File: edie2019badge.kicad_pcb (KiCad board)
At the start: 2 copper layers, 90 x 95.7 mm, 52 parts, among them CN2 2x2, CN3 2x2, CN4 2x2, CN5 1x6_vertical_sm, IC1 ESP-32-WROOM, IC2 AMS1117-3.3, SW1 switch_3x6, SW2 switch_3x6, SW3 switch_3x6

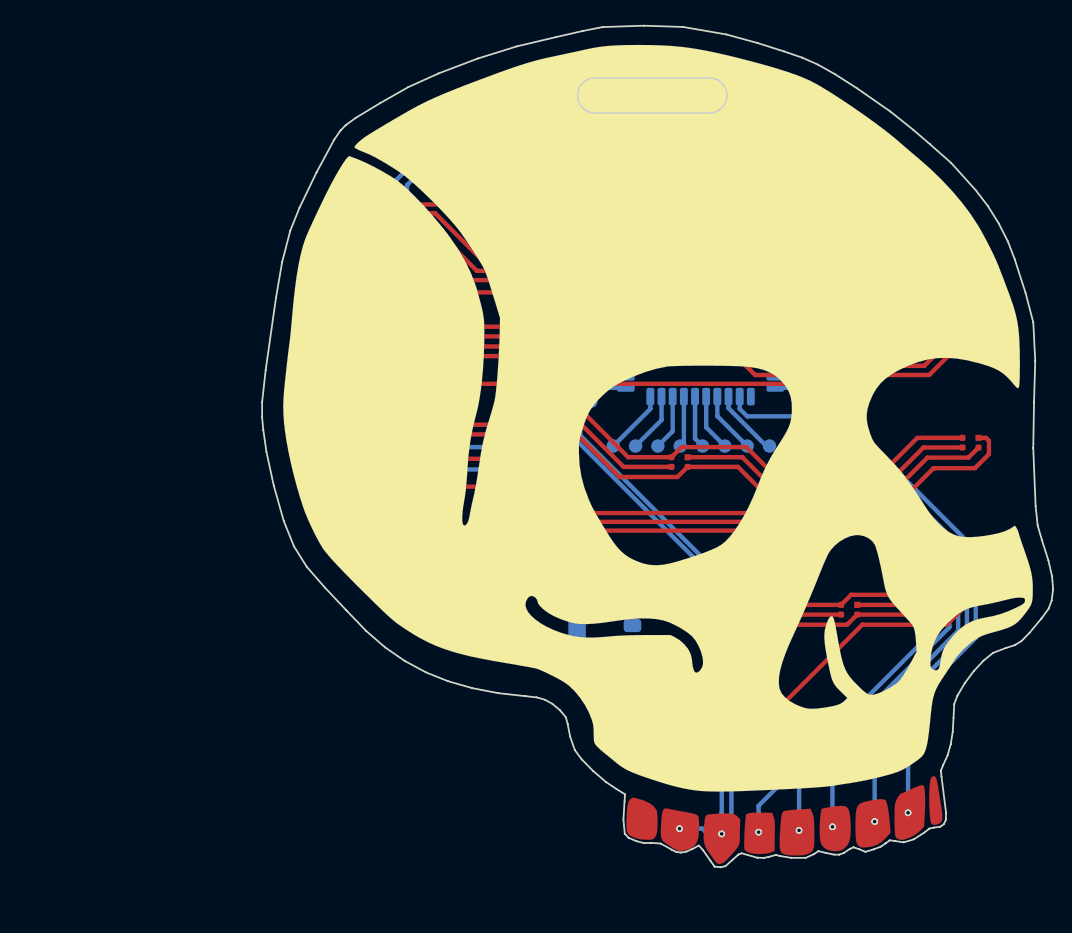
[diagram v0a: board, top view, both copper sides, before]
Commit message: trace layout complete for now, still missing some footprints
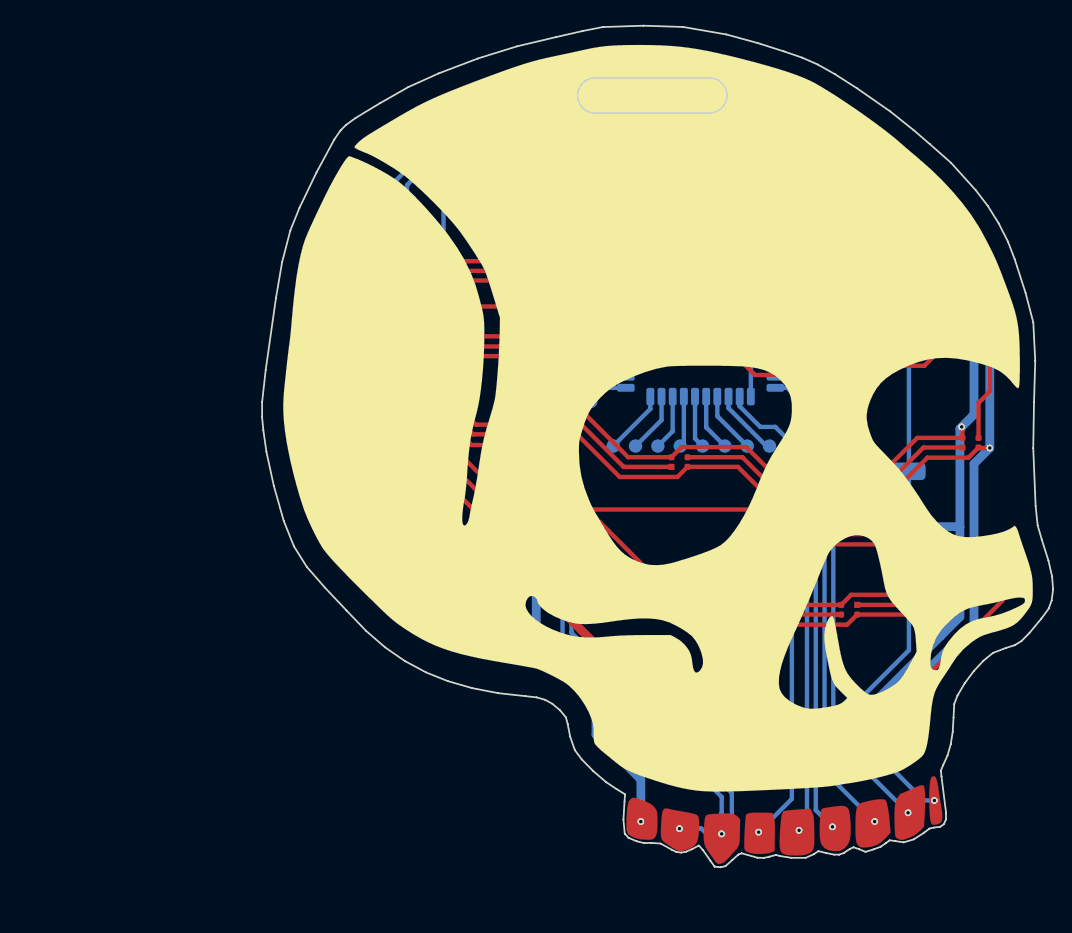
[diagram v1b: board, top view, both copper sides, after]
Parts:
- added TP18: test_point, PCB:test_point, B.Cu at (83.8, 71.1)
- moved IC2 37.5 mm to (120.0, 100.0), turned to 180 degrees
- moved TP1 31.0 mm to (87.0, 126.2)
- moved CN3 16.2 mm to (104.1, 106.7)
- moved TP17 7.62 mm to (83.8, 78.7)
- turned D13 to 180 degrees
- turned D14 to 180 degrees
- turned D15 to 180 degrees
- turned D16 to 180 degrees
- turned D17 to 180 degrees
- turned D23 to 180 degrees
- turned D24 to 180 degrees
- turned D25 to 180 degrees
- turned D5 to 180 degrees
- turned D6 to 180 degrees
- turned D7 to 180 degrees
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- renumbered D17 to D13, D16 to D14, D14 to D16, D13 to D17, D25 to D23, D23 to D25, D8 to D5, D7 to D6, D6 to D7, D5 to D8
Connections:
- D13 pad 1: Net-(D17-Pad1) -> Net-(D13-Pad1)
- D13 pad 3: Net-(D16-Pad1) -> Net-(D12-Pad1)
- D14 pad 1: Net-(D16-Pad1) -> Net-(D14-Pad1)
- D14 pad 3: Net-(D15-Pad1) -> Net-(D13-Pad1)
- D16 pad 1: Net-(D14-Pad1) -> Net-(D16-Pad1)
- D16 pad 3: Net-(D13-Pad1) -> Net-(D15-Pad1)
- D17 pad 1: Net-(D13-Pad1) -> Net-(D17-Pad1)
- D17 pad 3: Net-(D12-Pad1) -> Net-(D16-Pad1)
- D23 pad 1: Net-(D25-Pad1) -> Net-(D23-Pad1)
- D23 pad 3: Net-(D24-Pad1) -> Net-(D22-Pad1)
- D25 pad 1: Net-(D23-Pad1) -> Net-(D25-Pad1)
- D25 pad 3: Net-(D22-Pad1) -> Net-(D24-Pad1)
- D5 pad 1: Net-(D8-Pad1) -> Net-(D5-Pad1)
- D5 pad 3: Net-(D7-Pad1) -> Net-(D4-Pad1)
- D6 pad 1: Net-(D7-Pad1) -> Net-(D6-Pad1)
- D6 pad 3: Net-(D6-Pad1) -> Net-(D5-Pad1)
- D7 pad 1: Net-(D6-Pad1) -> Net-(D7-Pad1)
- D7 pad 3: Net-(D5-Pad1) -> Net-(D6-Pad1)
- D8 pad 1: Net-(D5-Pad1) -> Net-(D8-Pad1)
- D8 pad 3: Net-(D4-Pad1) -> Net-(D7-Pad1)
- TP17 pad 1: Net-(IC1-Pad37) -> Net-(IC1-Pad31)
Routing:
- net GND: track 372.3 -> 684.1 mm, vias 0 -> 12
- net +3V3: track 0.00 -> 191.6 mm, vias 0 -> 4
- net /LED strip/+5V_LEDs: track 368.0 -> 467.6 mm, vias 0 -> 6
- net Net-(D12-Pad1): track 90.1 -> 18.1 mm
- net Net-(D17-Pad1): track 84.0 -> 19.9 mm
- net Net-(D8-Pad1): track 75.6 -> 18.1 mm
- net Net-(D4-Pad1): track 67.2 -> 16.1 mm
- net /USB interface/RX: track 0.00 -> 43.9 mm
- net /LED strip/LED_strip_data: track 0.00 -> 41.4 mm, vias 0 -> 1
- net /USB interface/TX: track 0.00 -> 38.9 mm
- net Net-(D22-Pad1): track 54.6 -> 24.9 mm
- net /esp32/SCL: track 171.3 -> 154.6 mm
- net /esp32/SDA: track 167.7 -> 151.5 mm
- net /esp32/MOSI: track 69.8 -> 54.3 mm
- net Net-(CN5-Pad2): track 0.00 -> 13.2 mm
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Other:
- net class Default: clearance 0.2 -> 0.5
- rule trace_clearance: 0.2 -> 0.5

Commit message: layout completed
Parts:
- added C1: C, SMT:0603, B.Cu at (121.3, 106.5)
- added C2: C, SMT:0603, B.Cu at (107.2, 71.4)
- added C3: C, SMT:0603, B.Cu at (112.0, 57.5)
- added C4: C, SMT:0603, B.Cu at (122.0, 67.6)
- added C5: C, SMT:0603, B.Cu at (128.3, 80.9)
- added C6: C, SMT:0603, B.Cu at (128.3, 89.6)
- added C7: C, SMT:0603, B.Cu at (126.6, 106.5)
- added C8: C, SMT:0603, B.Cu at (117.6, 122.8)
- added D26: D, SMT:0603, B.Cu at (114.5, 100.0)
- added R1: R, SMT:0603, B.Cu at (112.5, 79.1)
- added R2: R, SMT:0603, B.Cu at (112.5, 77.5)
- added R3: R, SMT:0603, B.Cu at (118.0, 92.5)
- added R6: R, SMT:0603, B.Cu at (69.0, 69.0)
- added R7: R, SMT:0603, B.Cu at (65.0, 69.0)
- added T1: AO3401, SOT:SOT-23, B.Cu at (115.0, 92.5)
- added T2: AO3400, SOT:SOT-23, B.Cu at (116.0, 88.5)
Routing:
- net +5V_USB: track 0.00 -> 76.3 mm, vias 0 -> 4
- net /LED strip/LED_strip_enable: track 0.00 -> 46.6 mm, vias 0 -> 2
- net /LED strip/+5V_LEDs: track 467.6 -> 496.6 mm, vias 6 -> 7
- net +5V: track 0.00 -> 17.2 mm
- net GND: track 684.1 -> 700.6 mm, vias 12 -> 14
- net /USB interface/USB_power: track 0.00 -> 9.29 mm
- net /esp32/SCL: track 154.6 -> 159.4 mm
- net Net-(R3-Pad2): track 0.00 -> 3.95 mm
- net +3V3: track 191.6 -> 194.5 mm
- net /esp32/SDA: track 151.5 -> 150.7 mm

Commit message: added logos
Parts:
- added G***: LOGO, elite_dekkerz:hardware_crew, B.Cu at (92.0, 105.5)
- added G***: LOGO, elite_dekkerz:ELITE_dekkerz, B.Cu at (112.5, 118.5)

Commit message: started reworking layout
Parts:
- removed the D9 at (64.1, 83.2)
- added C10: C, SMT:0603, B.Cu at (28.3, 69.7)
- added C9: C, SMT:0603, B.Cu at (28.3, 70.7)
- added D18: WS2812B, SMT:2020, F.Cu at (52.5, 86.0)
- added R10: R, SMT:0603, B.Cu at (33.4, 70.7)
- added R11: R, SMT:0603, B.Cu at (30.9, 68.7)
- added R12: R, SMT:0603, B.Cu at (33.4, 69.7)
- added R4: R, SMT:0603, B.Cu at (30.9, 70.7)
- added R5: R, SMT:0603, B.Cu at (28.3, 68.7)
- added R8: R, SMT:0603, B.Cu at (30.9, 69.7)
- added R9: R, SMT:0603, B.Cu at (28.3, 67.7)
- added TP19: test_point, PCB:test_point, B.Cu at (73.2, 46.0)
- SW1, SW2, SW3: value switch_3x6 -> switch_3x4; footprint buttons:sw_3x6 -> buttons:sw_3x4
- moved TP1 81.8 mm to (70.7, 46.0)
- moved R3 71.6 mm to (56.8, 129.6)
- moved T1 71.6 mm to (53.8, 129.6)
- moved T2 71.6 mm to (54.8, 125.6)
- moved IC2 67.0 mm to (67.0, 141.0)
- moved C1 66.9 mm to (68.0, 147.0)
- moved D26 66.6 mm to (62.0, 141.0)
- moved TP17 61.4 mm to (109.2, 134.6)
- moved R2 59.3 mm to (62.0, 46.5)
- moved R1 59.3 mm to (62.0, 48.1)
- moved G*** 58.7 mm to (92.0, 63.5), turned to 180 degrees
- moved TP14 48.5 mm to (119.4, 129.5)
- moved TP13 47.2 mm to (116.8, 132.1)
- moved IC1 43.8 mm to (105.0, 122.0), turned to 270 degrees
- moved TP9 43.3 mm to (119.4, 127.0)
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- renumbered D25 to D1, D16 to D10, D15 to D11, D14 to D12, D12 to D14, D11 to D15, D10 to D16, D7 to D17, D8 to D19, D24 to D2, D2 to D20, D6 to D21, D5 to D22, D4 to D23, D3 to D24, D1 to D25, D23 to D3, D22 to D4, D21 to D5, D20 to D6, D19 to D7, D18 to D8, D17 to D9
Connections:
- C3 pad 1: /LED strip/+5V_LEDs -> /LED strip/+V_LEDs
- C4 pad 1: /LED strip/+5V_LEDs -> /LED strip/+V_LEDs
- C5 pad 1: /LED strip/+5V_LEDs -> /LED strip/+V_LEDs
- C6 pad 1: /LED strip/+5V_LEDs -> /LED strip/+V_LEDs
- C7 pad 1: /LED strip/+5V_LEDs -> /LED strip/+V_LEDs
- C8 pad 1: /LED strip/+5V_LEDs -> /LED strip/+V_LEDs
- D1 pad 1: Net-(D25-Pad1) -> Net-(D1-Pad1)
- D1 pad 3: Net-(D24-Pad1) -> /LED strip/LED_strip_data
- D1 pad 4: /LED strip/+5V_LEDs -> /LED strip/+V_LEDs
- D10 pad 1: Net-(D16-Pad1) -> Net-(D10-Pad1)
- D10 pad 3: Net-(D15-Pad1) -> Net-(D10-Pad3)
- D10 pad 4: /LED strip/+5V_LEDs -> /LED strip/+V_LEDs
- D11 pad 1: Net-(D15-Pad1) -> Net-(D11-Pad1)
- D11 pad 3: Net-(D14-Pad1) -> Net-(D10-Pad1)
- D11 pad 4: /LED strip/+5V_LEDs -> /LED strip/+V_LEDs
- D12 pad 1: Net-(D14-Pad1) -> Net-(D12-Pad1)
- D12 pad 3: Net-(D13-Pad1) -> Net-(D11-Pad1)
- D12 pad 4: /LED strip/+5V_LEDs -> /LED strip/+V_LEDs
- D13 pad 4: /LED strip/+5V_LEDs -> /LED strip/+V_LEDs
- D14 pad 1: Net-(D12-Pad1) -> Net-(D14-Pad1)
- D14 pad 3: Net-(D11-Pad1) -> Net-(D13-Pad1)
- D14 pad 4: /LED strip/+5V_LEDs -> /LED strip/+V_LEDs
- D15 pad 1: Net-(D11-Pad1) -> Net-(D15-Pad1)
- D15 pad 3: Net-(D10-Pad1) -> Net-(D14-Pad1)
- D15 pad 4: /LED strip/+5V_LEDs -> /LED strip/+V_LEDs
- D16 pad 1: Net-(D10-Pad1) -> Net-(D16-Pad1)
- D16 pad 3: Net-(D10-Pad3) -> Net-(D15-Pad1)
- D16 pad 4: /LED strip/+5V_LEDs -> /LED strip/+V_LEDs
- D17 pad 1: Net-(D7-Pad1) -> Net-(D17-Pad1)
- D17 pad 3: Net-(D6-Pad1) -> Net-(D16-Pad1)
- D17 pad 4: /LED strip/+5V_LEDs -> /LED strip/+V_LEDs
- D19 pad 1: Net-(D8-Pad1) -> Net-(D19-Pad1)
- D19 pad 3: Net-(D7-Pad1) -> Net-(D18-Pad1)
- D19 pad 4: /LED strip/+5V_LEDs -> /LED strip/+V_LEDs
- D2 pad 1: Net-(D24-Pad1) -> Net-(D2-Pad1)
- D2 pad 3: Net-(D23-Pad1) -> Net-(D1-Pad1)
- D2 pad 4: /LED strip/+5V_LEDs -> /LED strip/+V_LEDs
- D20 pad 1: Net-(D2-Pad1) -> Net-(D20-Pad1)
- D20 pad 3: Net-(D1-Pad1) -> Net-(D19-Pad1)
- D20 pad 4: /LED strip/+5V_LEDs -> /LED strip/+V_LEDs
- D21 pad 1: Net-(D6-Pad1) -> Net-(D21-Pad1)
- D21 pad 3: Net-(D5-Pad1) -> Net-(D20-Pad1)
- D21 pad 4: /LED strip/+5V_LEDs -> /LED strip/+V_LEDs
- D22 pad 1: Net-(D5-Pad1) -> Net-(D22-Pad1)
- D22 pad 3: Net-(D4-Pad1) -> Net-(D21-Pad1)
- D22 pad 4: /LED strip/+5V_LEDs -> /LED strip/+V_LEDs
- D23 pad 1: Net-(D4-Pad1) -> Net-(D23-Pad1)
- D23 pad 3: Net-(D3-Pad1) -> Net-(D22-Pad1)
- D23 pad 4: /LED strip/+5V_LEDs -> /LED strip/+V_LEDs
- D24 pad 1: Net-(D3-Pad1) -> Net-(D24-Pad1)
- D24 pad 3: Net-(D2-Pad1) -> Net-(D23-Pad1)
- D24 pad 4: /LED strip/+5V_LEDs -> /LED strip/+V_LEDs
- D25 pad 1: Net-(D1-Pad1) -> Net-(D25-Pad1)
- D25 pad 3: /LED strip/LED_strip_data -> Net-(D24-Pad1)
- D25 pad 4: /LED strip/+5V_LEDs -> /LED strip/+V_LEDs
- D3 pad 1: Net-(D23-Pad1) -> Net-(D3-Pad1)
- D3 pad 3: Net-(D22-Pad1) -> Net-(D2-Pad1)
- D3 pad 4: /LED strip/+5V_LEDs -> /LED strip/+V_LEDs
- D4 pad 1: Net-(D22-Pad1) -> Net-(D4-Pad1)
- D4 pad 3: Net-(D21-Pad1) -> Net-(D3-Pad1)
- D4 pad 4: /LED strip/+5V_LEDs -> /LED strip/+V_LEDs
- D5 pad 1: Net-(D21-Pad1) -> Net-(D5-Pad1)
- D5 pad 3: Net-(D20-Pad1) -> Net-(D4-Pad1)
- D5 pad 4: /LED strip/+5V_LEDs -> /LED strip/+V_LEDs
- D6 pad 1: Net-(D20-Pad1) -> Net-(D6-Pad1)
- D6 pad 3: Net-(D19-Pad1) -> Net-(D5-Pad1)
- D6 pad 4: /LED strip/+5V_LEDs -> /LED strip/+V_LEDs
- D7 pad 1: Net-(D19-Pad1) -> Net-(D7-Pad1)
- D7 pad 3: Net-(D18-Pad1) -> Net-(D6-Pad1)
- D7 pad 4: /LED strip/+5V_LEDs -> /LED strip/+V_LEDs
- D8 pad 1: Net-(D18-Pad1) -> Net-(D8-Pad1)
- D8 pad 3: Net-(D17-Pad1) -> Net-(D7-Pad1)
- D8 pad 4: /LED strip/+5V_LEDs -> /LED strip/+V_LEDs
- D9 pad 1: Net-(D17-Pad1) -> Net-(D10-Pad3)
- D9 pad 3: Net-(D16-Pad1) -> Net-(D8-Pad1)
- D9 pad 4: /LED strip/+5V_LEDs -> /LED strip/+V_LEDs
- IC1 pad 13: /esp32/CLK -> Net-(IC1-Pad13)
- IC1 pad 14: /esp32/MISO -> Net-(IC1-Pad14)
- IC1 pad 16: /esp32/MOSI -> Net-(IC1-Pad16)
- IC1 pad 29: /LED strip/LED_strip_data -> Net-(IC1-Pad29)
- IC1 pad 30: /LED strip/LED_strip_enable -> /esp32/SCK
- IC1 pad 31: Net-(IC1-Pad31) -> /esp32/MISO
- IC1 pad 33: /esp32/SDA -> /esp32/MOSI
- IC1 pad 36: /esp32/SCL -> /esp32/SDA
- IC1 pad 37: Net-(IC1-Pad37) -> /esp32/SCL
- IC1 pad 7: Net-(IC1-Pad7) -> /esp32/battery_charging
- IC1 pad 8: Net-(IC1-Pad8) -> /LED strip/LED_strip_data
- IC1 pad 9: Net-(IC1-Pad9) -> /LED strip/LED_strip_enable
- IC2 pad 3: +5V -> VCC
- R3 pad 1: +5V -> VCC
- SKL666 pad 2: /esp32/RX2 -> /esp32/SCL
- SKL666 pad 3: /esp32/TX2 -> /esp32/SDA
- SKL666 pad 4: /esp32/SCL -> /esp32/MOSI
- SKL666 pad 5: /esp32/SDA -> /esp32/MISO
- SKL666 pad 6: /esp32/MOSI -> /esp32/SCK
- SKL666 pad 7: /esp32/MISO -> /esp32/TX2
- SKL666 pad 8: /esp32/CLK -> /esp32/RX2
- SW1 pad 1: Net-(IC1-Pad7) -> Net-(IC1-Pad25)
- SW1 pad 2: GND -> Net-(IC1-Pad25)
- SW2 pad 1: Net-(IC1-Pad8) -> Net-(IC1-Pad16)
- SW2 pad 2: GND -> Net-(IC1-Pad16)
- SW3 pad 1: Net-(IC1-Pad9) -> Net-(IC1-Pad23)
- SW3 pad 2: GND -> Net-(IC1-Pad23)
- T1 pad 2: +5V -> VCC
- T1 pad 3: /LED strip/+5V_LEDs -> /LED strip/+V_LEDs
- TP13 pad 1: Net-(IC1-Pad23) -> Net-(IC1-Pad26)
- TP15 pad 1: Net-(IC1-Pad25) -> Net-(IC1-Pad14)
- TP16 pad 1: Net-(IC1-Pad26) -> Net-(IC1-Pad13)
- TP17 pad 1: Net-(IC1-Pad31) -> Net-(IC1-Pad29)
- TP18 pad 1: Net-(IC1-Pad37) -> /LED strip/+V_LEDs
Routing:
- net /LED strip/+5V_LEDs: track 496.6 -> 0.00 mm, vias 7 -> 0
- net /LED strip/+V_LEDs: track 0.00 -> 403.3 mm, vias 0 -> 6
- net GND: track 700.6 -> 428.4 mm, vias 14 -> 6
- net +3V3: track 194.5 -> 0.00 mm, vias 4 -> 0
- net /esp32/SCL: track 159.4 -> 8.70 mm, vias 2 -> 1
- net /esp32/SDA: track 150.7 -> 7.84 mm, vias 3 -> 1
- net +5V_USB: track 76.3 -> 0.00 mm, vias 4 -> 0
- net /esp32/RX2: track 73.8 -> 12.4 mm
- net Net-(IC1-Pad16): track 0.00 -> 61.4 mm, vias 0 -> 1
- net /esp32/battery_charging: track 0.00 -> 60.5 mm
- net /esp32/TX2: track 68.0 -> 10.4 mm
- net /esp32/CLK: track 56.9 -> 0.00 mm, vias 1 -> 0
- net Net-(IC1-Pad7): track 47.7 -> 0.00 mm, vias 1 -> 0
- net /esp32/MISO: track 54.8 -> 7.97 mm
- net /esp32/MOSI: track 54.3 -> 7.48 mm
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
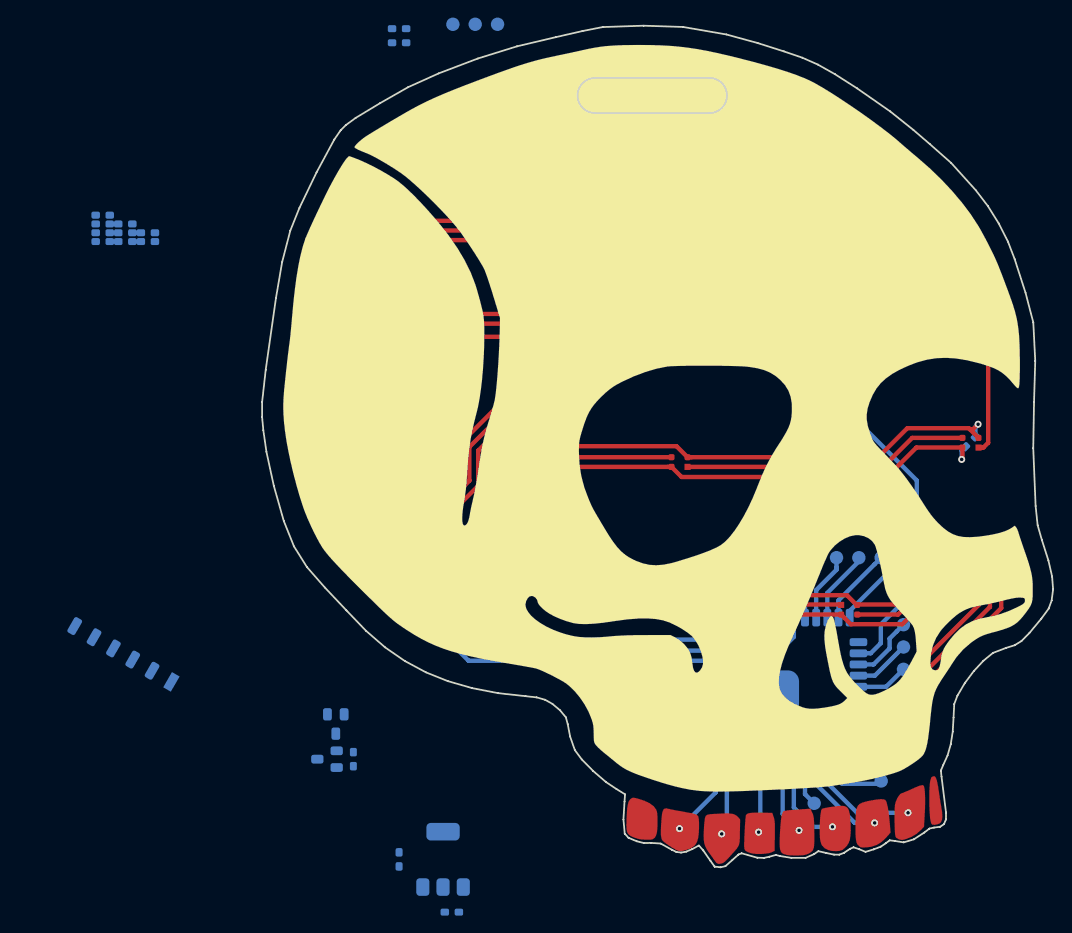
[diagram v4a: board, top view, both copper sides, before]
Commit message: started battery protection circuit layout
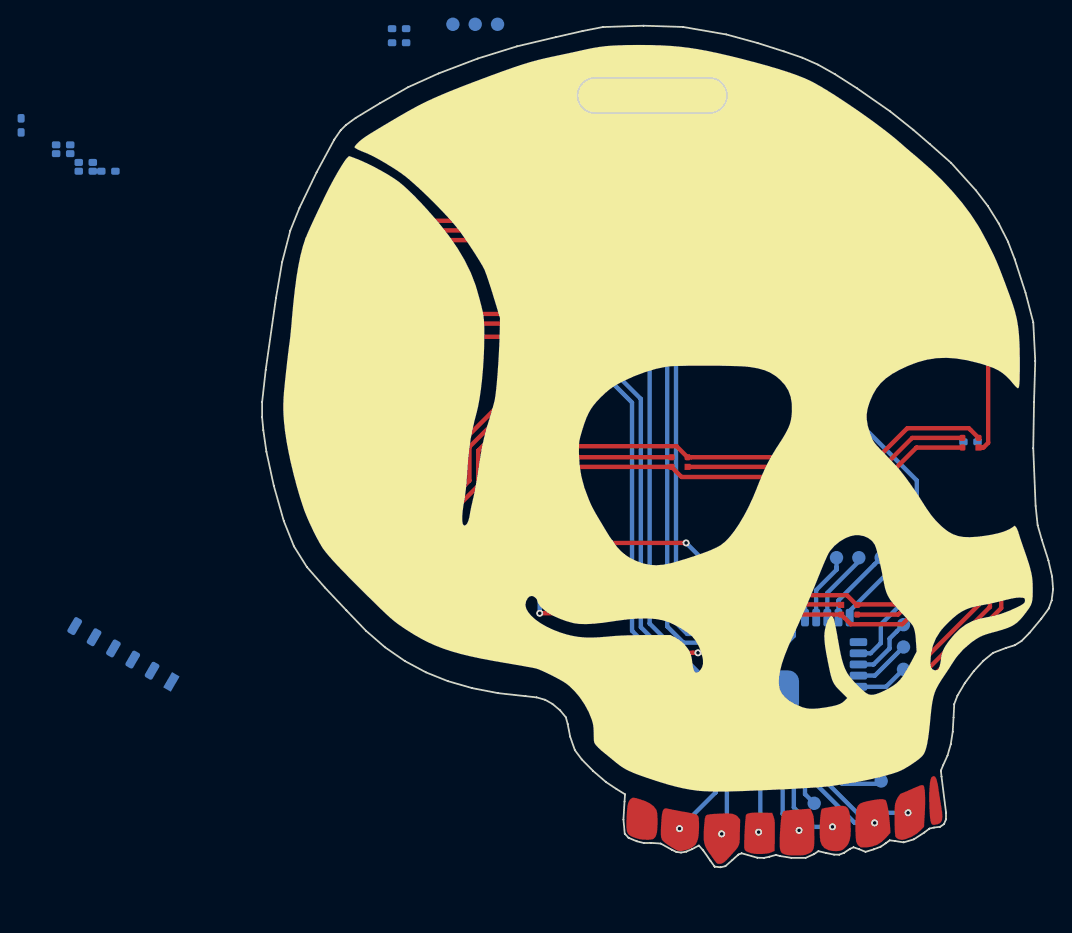
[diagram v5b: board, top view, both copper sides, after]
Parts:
- removed D26: D, SMT:0603
- added IC4: DW01, SOT:SOT-23-6, B.Cu at (53.0, 98.0)
- added T3: FS8205A, TSSOP:TSSOP-8, B.Cu at (57.0, 98.0)
- IC2: value AMS1117-3.3 -> XC6206P332MR; footprint SOT:SOT-223 -> SOT:SOT-23
- moved C1 43.9 mm to (85.0, 106.5), turned to 180 degrees
- moved R12 37.8 mm to (53.0, 102.0), turned to 270 degrees
- moved IC2 36.3 mm to (85.0, 109.5), turned to 0 degrees
- moved C10 35.7 mm to (53.5, 95.0)
- moved T1 33.8 mm to (81.0, 109.5), turned to 0 degrees
- moved R3 33.5 mm to (81.0, 106.5), turned to 180 degrees
- moved R11 32.2 mm to (52.5, 92.5), turned to 270 degrees
- moved T2 27.4 mm to (77.0, 109.5), turned to 180 degrees
- moved C9 16.2 mm to (19.0, 57.5), turned to 90 degrees
- moved R4 9.18 mm to (26.4, 62.7)
- moved R5 9.18 mm to (23.8, 60.7)
- moved R8 9.18 mm to (26.4, 61.7)
- moved R9 9.18 mm to (23.8, 59.7)
- moved R10 9.18 mm to (28.9, 62.7)
- turned C3 to 180 degrees
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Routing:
- net /USB interface/TX: track 0.00 -> 74.2 mm
- net /USB interface/RX: track 0.00 -> 73.9 mm
- net Net-(IC1-Pad25): track 0.00 -> 69.8 mm, vias 0 -> 1
- net /USB interface/USB_power: track 0.00 -> 52.6 mm, vias 0 -> 1
- net /LED strip/LED_strip_enable: track 69.1 -> 38.0 mm, vias 0 -> 2
- net +3V3: track 0.00 -> 25.2 mm, vias 0 -> 2
- net /LED strip/+V_LEDs: track 403.3 -> 388.3 mm, vias 6 -> 0
- net GND: track 428.4 -> 417.4 mm, vias 6 -> 0
- net Net-(IC4-Pad3): track 0.00 -> 9.30 mm
- net Net-(BAT1-Pad2): track 0.00 -> 8.70 mm
- net /esp32/battery_charging: track 60.5 -> 54.4 mm, vias 0 -> 1
- net VCC: track 0.00 -> 5.93 mm
- net Net-(R3-Pad2): track 0.00 -> 5.01 mm
- net Net-(IC1-Pad16): track 61.4 -> 65.6 mm
- net /LED strip/LED_strip_data: track 27.0 -> 24.2 mm
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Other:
- net class Default: clearance 0.5 -> 0.2
- rule trace_clearance: 0.5 -> 0.2
